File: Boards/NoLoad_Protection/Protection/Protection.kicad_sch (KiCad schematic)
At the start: 25 parts

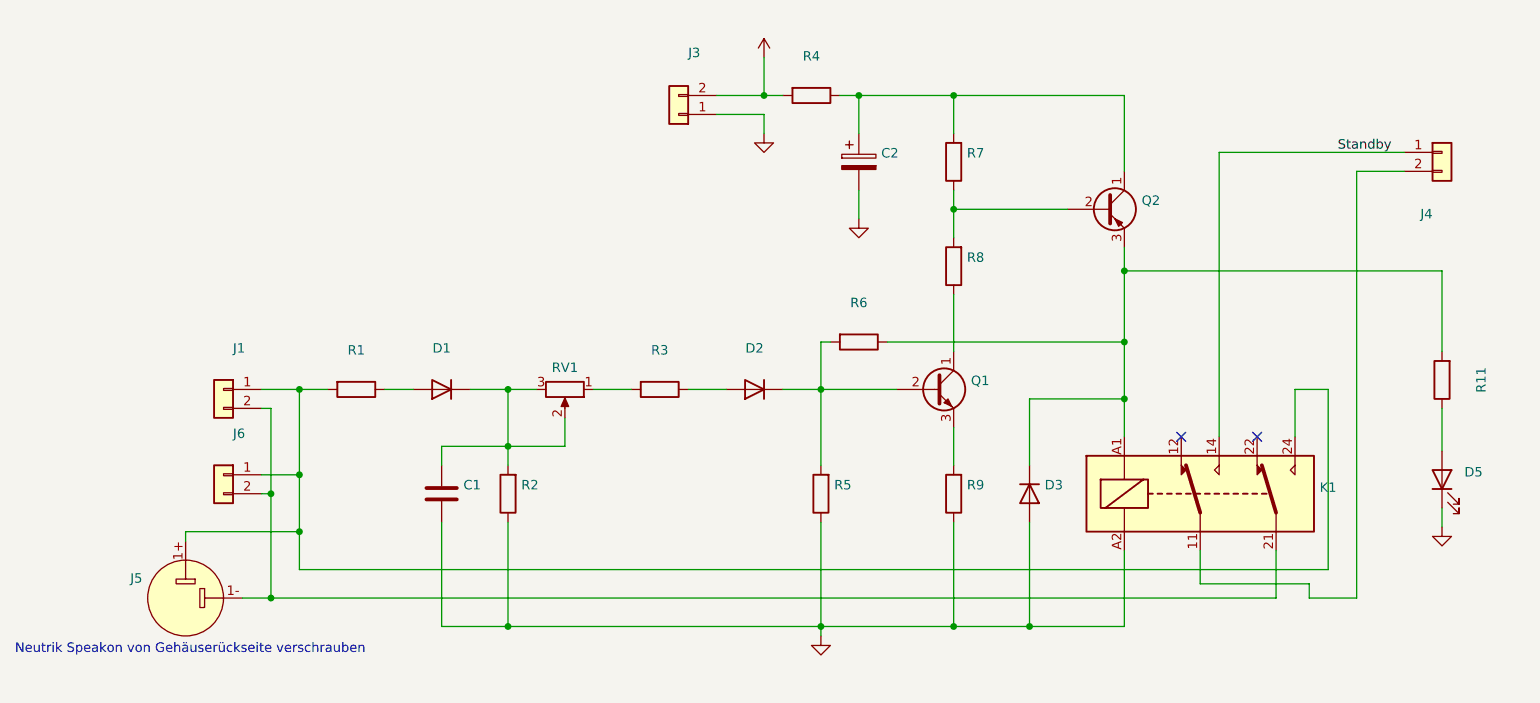
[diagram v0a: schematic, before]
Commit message: 6.3V, 400V und 400V Regler Boards bestellt
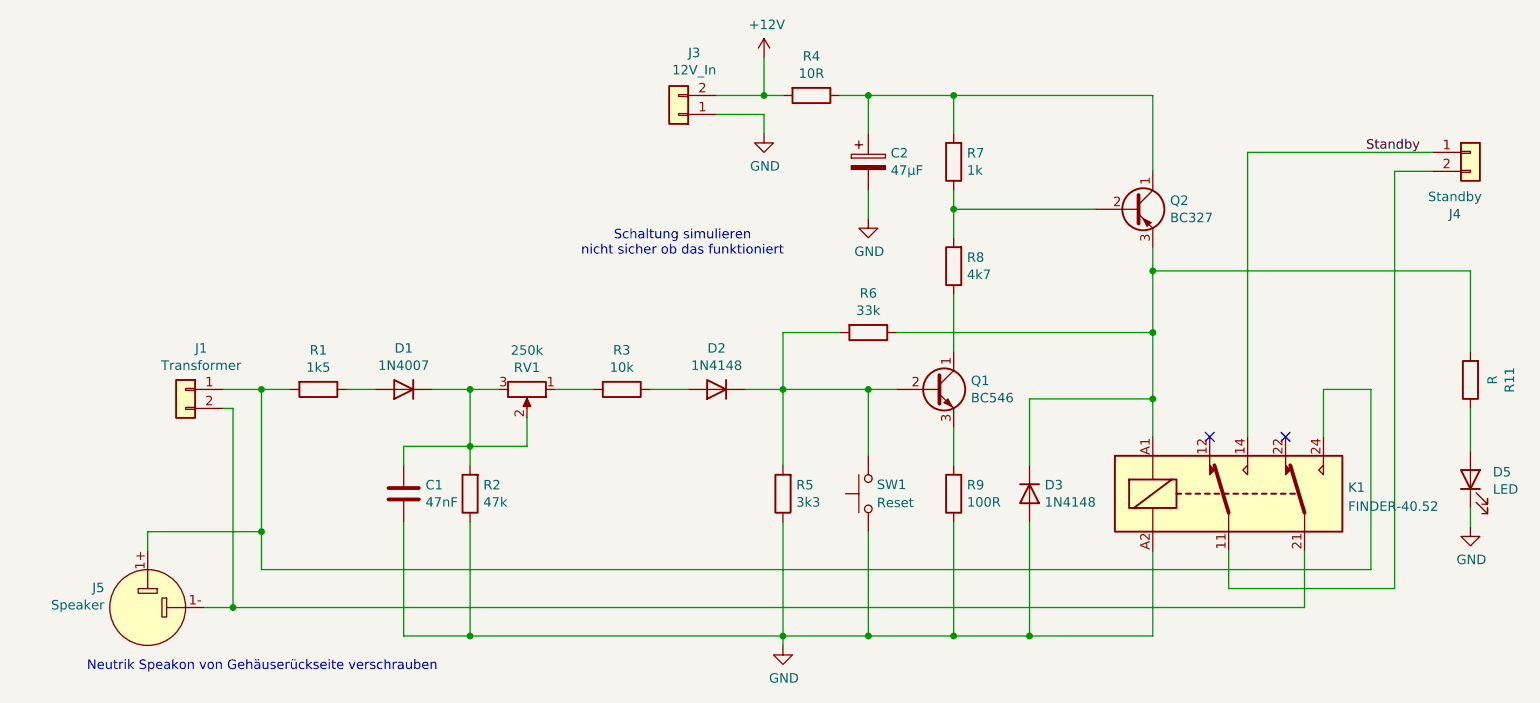
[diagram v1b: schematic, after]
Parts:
- removed J6: (no value), symbol Connector_Generic:Conn_01x02
- added SW1: Reset, Button_Switch_THT:SW_PUSH_6mm_H7.3mm, symbol Switch:SW_Push
- C1: value (none) -> 47nF; footprint (none) -> Capacitor_THT:C_Disc_D3.4mm_W2.1mm_P2.50mm
- C2: value (none) -> 47µF; footprint (none) -> Capacitor_THT:CP_Radial_D5.0mm_P2.50mm
- D1: value (none) -> 1N4007; footprint (none) -> Diode_THT:D_DO-41_SOD81_P10.16mm_Horizontal
- D2, D3: value (none) -> 1N4148; footprint (none) -> Diode_THT:D_DO-35_SOD27_P10.16mm_Horizontal
- D5: value (none) -> LED; footprint (none) -> LED_THT:LED_D3.0mm
- J1: value (none) -> Transformer; footprint (none) -> Connector_TE-Connectivity:TE_MATE-N-LOK_1-770866-x_1x02_P4.14mm_Vertical
- J3: value (none) -> 12V_In; footprint (none) -> Connector_Molex:Molex_KK-254_AE-6410-02A_1x02_P2.54mm_Vertical
- J4: value (none) -> Standby; footprint (none) -> Connector_Molex:Molex_KK-254_AE-6410-02A_1x02_P2.54mm_Vertical
- J5: value (none) -> Speaker; footprint (none) -> Connector_Audio:Jack_speakON_Neutrik_NL2MD-V_Vertical
- K1: value (none) -> FINDER-40.52; footprint (none) -> Relay_THT:Relay_DPDT_Finder_40.52
- Q1: value (none) -> BC546; footprint (none) -> Package_TO_SOT_THT:TO-92_Inline
- Q2: value (none) -> BC327; footprint (none) -> Package_TO_SOT_THT:TO-92_Inline
- R1: value (none) -> 1k5; footprint (none) -> Resistor_THT:R_Axial_DIN0207_L6.3mm_D2.5mm_P10.16mm_Horizontal
- R11: value (none) -> R; footprint (none) -> Resistor_THT:R_Axial_DIN0207_L6.3mm_D2.5mm_P10.16mm_Horizontal
- R2: value (none) -> 47k; footprint (none) -> Resistor_THT:R_Axial_DIN0207_L6.3mm_D2.5mm_P10.16mm_Horizontal
- R3: value (none) -> 10k; footprint (none) -> Resistor_THT:R_Axial_DIN0207_L6.3mm_D2.5mm_P10.16mm_Horizontal
- R4: value (none) -> 10R; footprint (none) -> Resistor_THT:R_Axial_DIN0207_L6.3mm_D2.5mm_P10.16mm_Horizontal
- R5: value (none) -> 3k3; footprint (none) -> Resistor_THT:R_Axial_DIN0207_L6.3mm_D2.5mm_P10.16mm_Horizontal
- R6: value (none) -> 33k; footprint (none) -> Resistor_THT:R_Axial_DIN0207_L6.3mm_D2.5mm_P10.16mm_Horizontal
- R7: value (none) -> 1k; footprint (none) -> Resistor_THT:R_Axial_DIN0207_L6.3mm_D2.5mm_P10.16mm_Horizontal
- R8: value (none) -> 4k7; footprint (none) -> Resistor_THT:R_Axial_DIN0207_L6.3mm_D2.5mm_P10.16mm_Horizontal
- R9: value (none) -> 100R; footprint (none) -> Resistor_THT:R_Axial_DIN0207_L6.3mm_D2.5mm_P10.16mm_Horizontal
- RV1: value (none) -> 250k; footprint (none) -> Potentiometer_THT:Potentiometer_Piher_PT-10-V10_Vertical_Hole
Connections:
- net GND: now also SW1.1
- net at D2.1 (K), Q1.2 (B), R5.2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: now also SW1.2
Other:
- note added: "Schaltung simulieren nicht sicher ob das funktioniert"
- moved on the sheet: C1, C2, D1, D2, D5, J1, J4, J5, K1, Q2, R1, R11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
